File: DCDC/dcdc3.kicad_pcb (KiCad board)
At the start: 2 copper layers, 90 x 80 mm, 84 parts, among them M1-1 30V 60A, M1-2 30V 60A, M1-3 30V 60A, M2-1 30V 35A, M2-2 30V 35A, M2-3 30V 35A, U1 LM5145RGYR, U2 LM5145RGYR, U3 LM5145RGYR

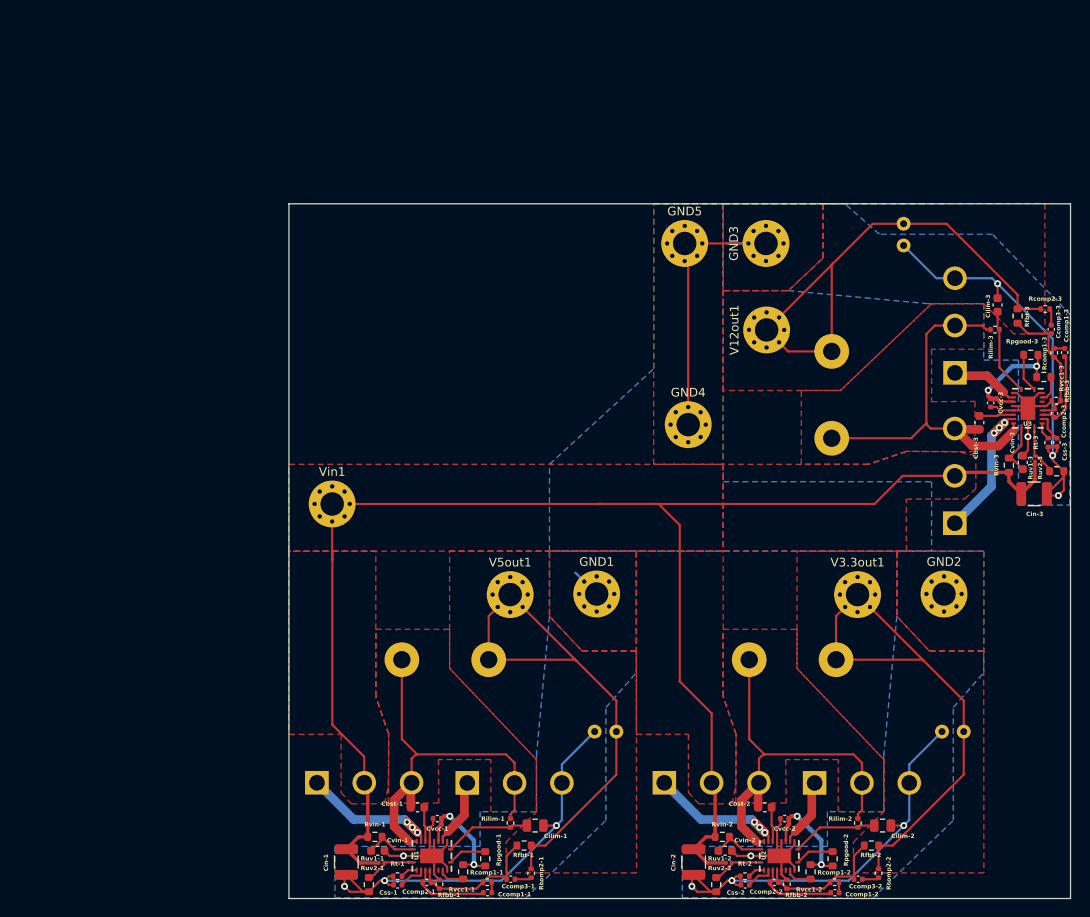
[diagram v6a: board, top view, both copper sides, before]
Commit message: DCDC fix unavailable parts, BMS redesign, handle fix, rearrange top half
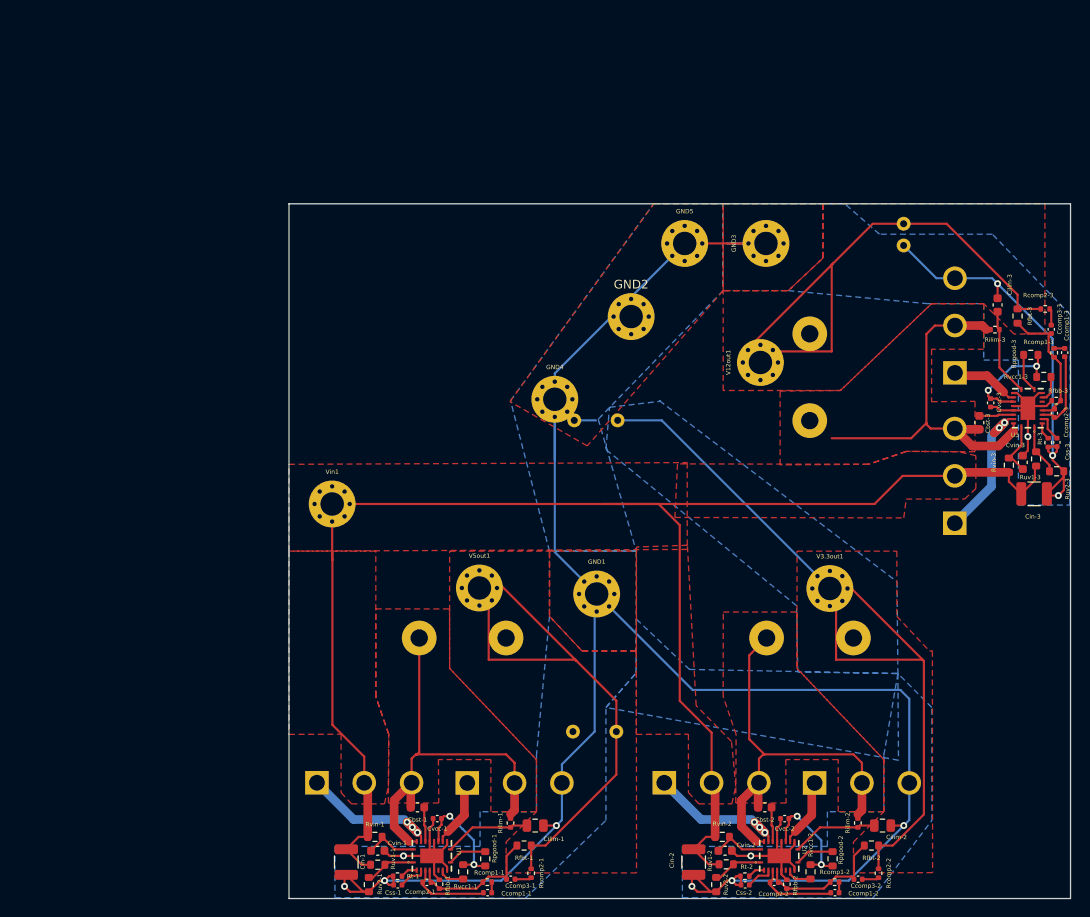
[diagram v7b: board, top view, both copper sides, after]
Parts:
- Cout-1, Cout-2: footprint Capacitor_THT:C_Radial_D6.3mm_H5.0mm_P2.50mm -> Capacitor_THT:C_Radial_D10.0mm_H12.5mm_P5.00mm
- Ruv1-1, Ruv1-2, Ruv1-3: footprint Resistor_SMD:R_0201_0603Metric -> Resistor_SMD:R_0603_1608Metric
- moved Cout-2 53.6 mm to (97.8, 84.9)
- moved GND2 48.1 mm to (99.4, 73.0)
- moved GND4 15.6 mm to (90.6, 82.5)
- moved V12out1 3.82 mm to (114.3, 78.3)
- moved V5out1 3.62 mm to (81.9, 104.2)
- moved V3.3out1 3.26 mm to (122.3, 104.3)
- moved L1-3 3.24 mm to (120.0, 80.0)
- moved L1-1 3.20 mm to (80.0, 110.0)
- moved L1-2 3.20 mm to (120.0, 110.0)
- moved Ruv1-1 0.47 mm to (70.2, 136.1)
- moved Ruv1-2 0.33 mm to (110.4, 136.1)
- moved Ruv1-3 0.14 mm to (146.0, 89.4)
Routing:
- net /12V/GND: track 249.0 -> 345.5 mm
- net /3.3V/V3.3out: track 60.4 -> 93.0 mm
- net /12V/V12out: track 60.4 -> 64.9 mm
- net /5V/V5out: track 60.4 -> 64.7 mm
- net Net-(U2-SW): track 46.4 -> 49.7 mm
- net /12V/Vin: track 194.7 -> 191.8 mm
- net Net-(U1-SW): track 46.4 -> 48.3 mm
- net Net-(U3-HO): vias 3 -> 2
- added copper zone on B.Cu, net /3.3V/V3.3out
